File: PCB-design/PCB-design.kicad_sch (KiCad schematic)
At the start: 1 part, among them U1 UCC28070DW

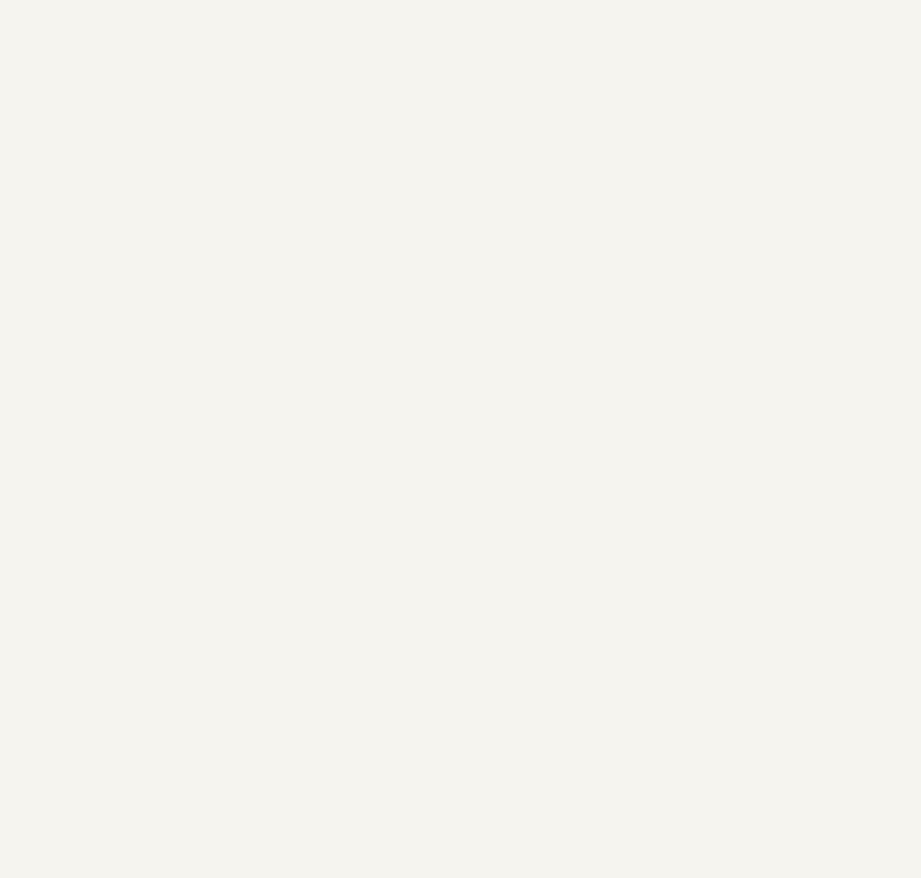
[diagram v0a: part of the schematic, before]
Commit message: New pin headers
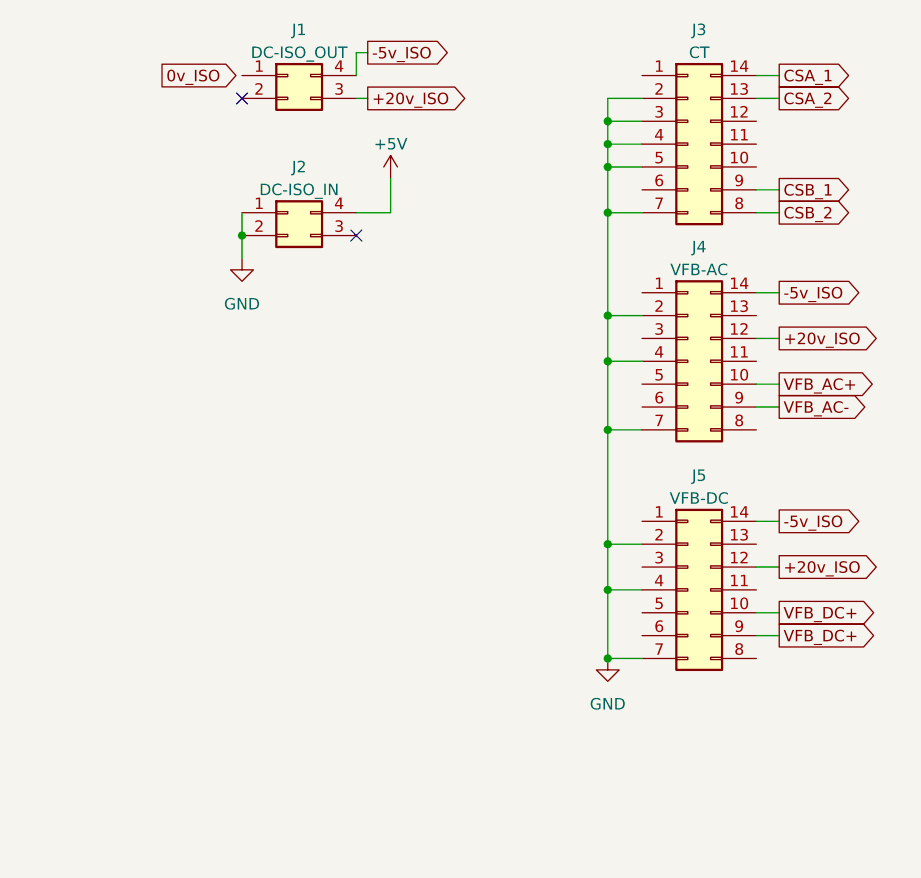
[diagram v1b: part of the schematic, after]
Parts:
- added J1: DC-ISO_OUT, symbol Connector_Generic:Conn_02x02_Counter_Clockwise
- added J2: DC-ISO_IN, symbol Connector_Generic:Conn_02x02_Counter_Clockwise
- added J3: CT, symbol Connector_Generic:Conn_02x07_Counter_Clockwise
- added J4: VFB-AC, symbol Connector_Generic:Conn_02x07_Counter_Clockwise
- added J5: VFB-DC, symbol Connector_Generic:Conn_02x07_Counter_Clockwise
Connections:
- new net +20v_ISO: J1.3 (Pin_3), J4.12 (Pin_12), J5.12 (Pin_12)
- new net +5V: J2.4 (Pin_4)
- new net -5v_ISO: J1.4 (Pin_4), J4.14 (Pin_14), J5.14 (Pin_14)
- new net CSA_1: J3.14 (Pin_14)
- new net CSA_2: J3.13 (Pin_13)
- new net CSB_1: J3.9 (Pin_9)
- new net CSB_2: J3.8 (Pin_8)
- new net GND: J2.1 (Pin_1), J2.2 (Pin_2), J3.2 (Pin_2), J3.3 (Pin_3), J3.4 (Pin_4), J3.5 (Pin_5), J3.7 (Pin_7), J4.2 (Pin_2), J4.4 (Pin_4), J4.7 (Pin_7), J5.2 (Pin_2), J5.4 (Pin_4), J5.7 (Pin_7)
- new net VFB_AC+: J4.10 (Pin_10)
- new net VFB_AC-: J4.9 (Pin_9)
- new net VFB_DC+: J5.10 (Pin_10), J5.9 (Pin_9)
- no-connect marks 0 -> 2

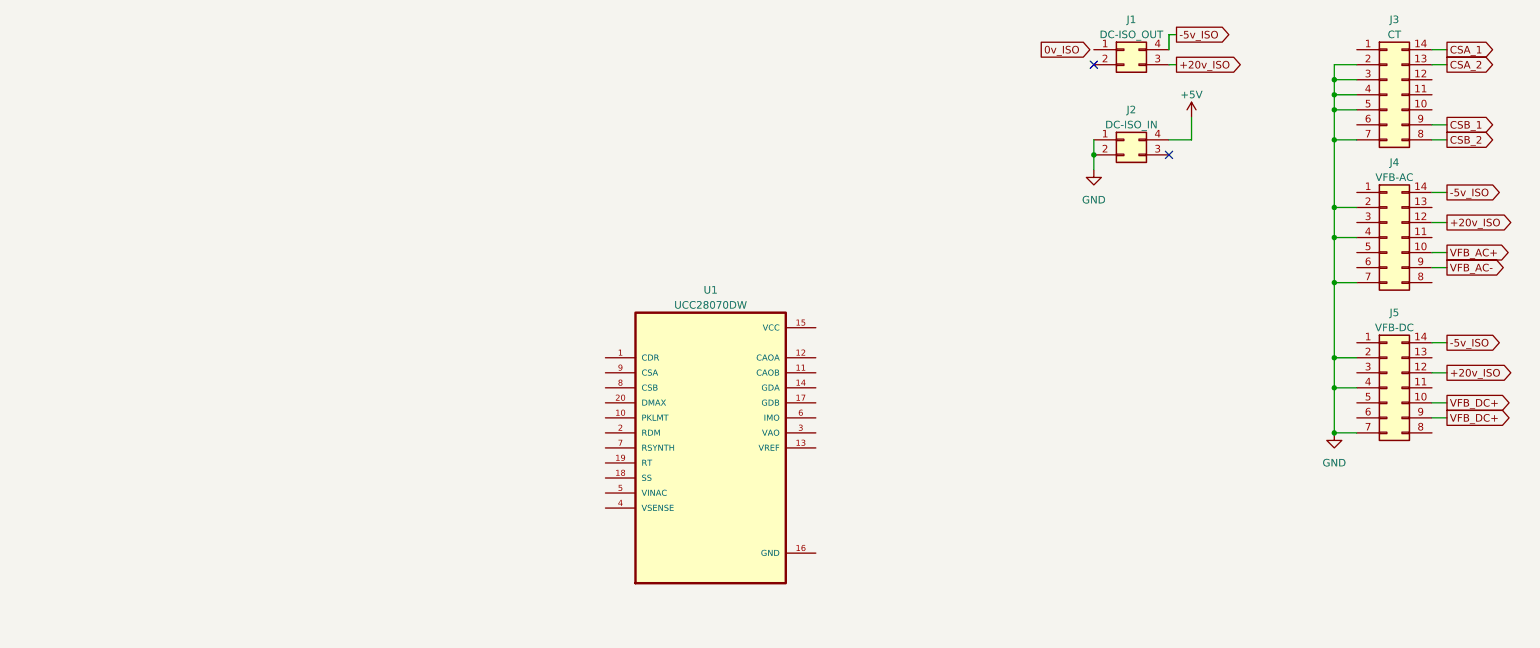
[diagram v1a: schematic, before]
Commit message: boost converter added: should probably double check
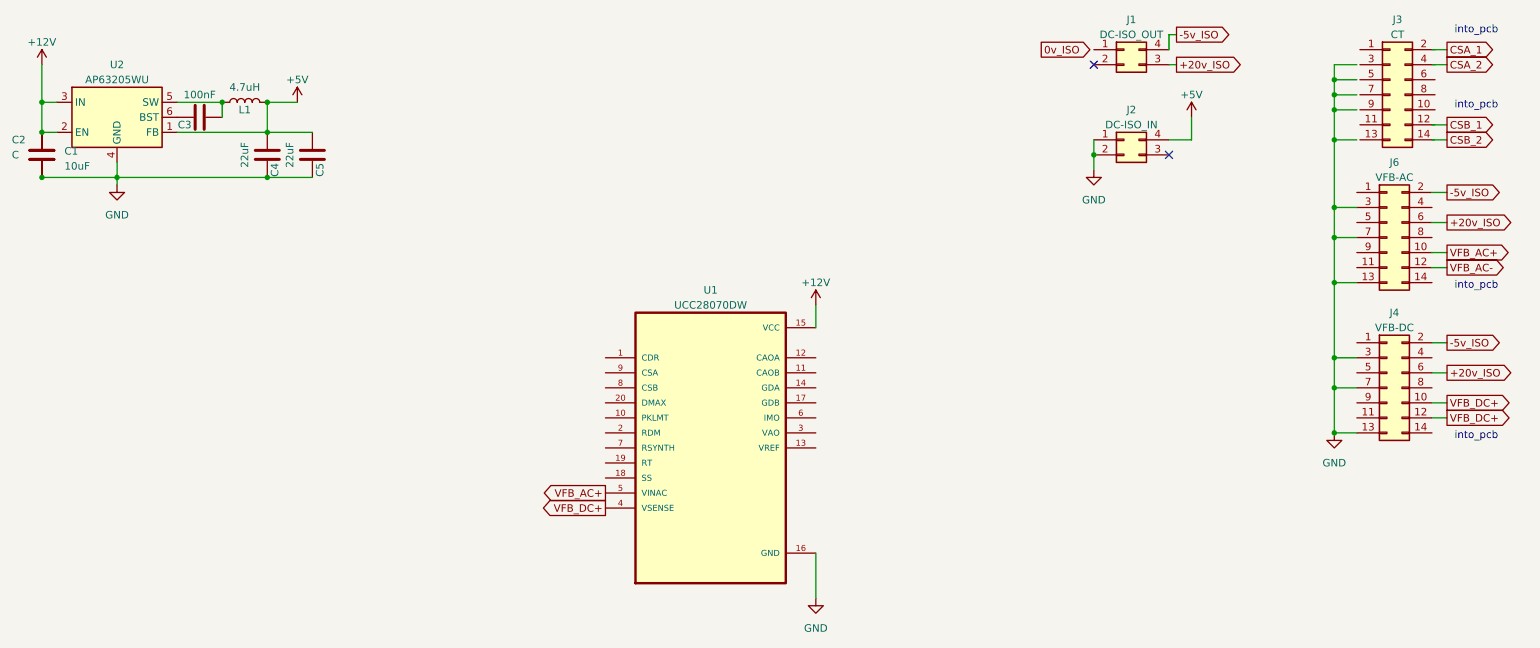
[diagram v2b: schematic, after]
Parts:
- removed J3: CT, symbol Connector_Generic:Conn_02x07_Counter_Clockwise
- removed J4: VFB-AC, symbol Connector_Generic:Conn_02x07_Counter_Clockwise
- removed J5: VFB-DC, symbol Connector_Generic:Conn_02x07_Counter_Clockwise
- added C1: 10uF, symbol Device:C
- added C2: C, symbol Device:C
- added C3: 100nF, symbol Device:C
- added C4, C5: 22uF, symbol Device:C
- added J3: CT, symbol Connector_Generic:Conn_02x07_Odd_Even
- added J4: VFB-DC, symbol Connector_Generic:Conn_02x07_Odd_Even
- added J6: VFB-AC, symbol Connector_Generic:Conn_02x07_Odd_Even
- added L1: 4.7uH, symbol Device:L
- added U2: AP63205WU, Package_TO_SOT_SMD:TSOT-23-6, symbol Regulator_Switching:AP63205WU
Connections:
- net +20v_ISO: now also J4.6 (Pin_6), J6.6 (Pin_6)
- net +5V: now also C4.2, C5.2, L1.2, U2.1 (FB)
- net -5v_ISO: now also J4.2 (Pin_2), J6.2 (Pin_2)
- net GND: now also U1.16 (GND), C1.2, C2.2, C4.1, C5.1, J4.13 (Pin_13), J4.3 (Pin_3), J4.7 (Pin_7), J6.13 (Pin_13), J6.3 (Pin_3), J6.7 (Pin_7), U2.4 (GND)
- net VFB_AC+: now also U1.5 (VINAC), J6.10 (Pin_10)
- net VFB_AC-: now also J6.12 (Pin_12)
- net VFB_DC+: now also U1.4 (VSENSE), J4.10 (Pin_10), J4.12 (Pin_12)
- net +12V: now reaches U1.15 (VCC)
- net +12V: now also C1.1, C2.1, U2.2 (EN), U2.3 (IN)
- new net: C3.2, L1.1, U2.5 (SW)
- new net: C3.1, U2.6 (BST)
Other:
- note added: "into_pcb"

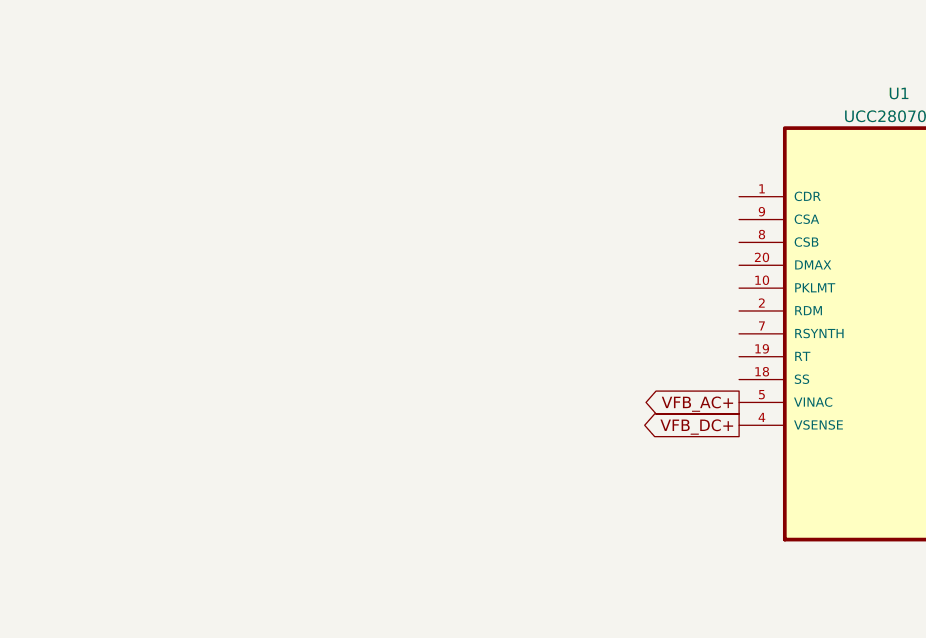
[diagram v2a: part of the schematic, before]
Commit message: structuring IC pins
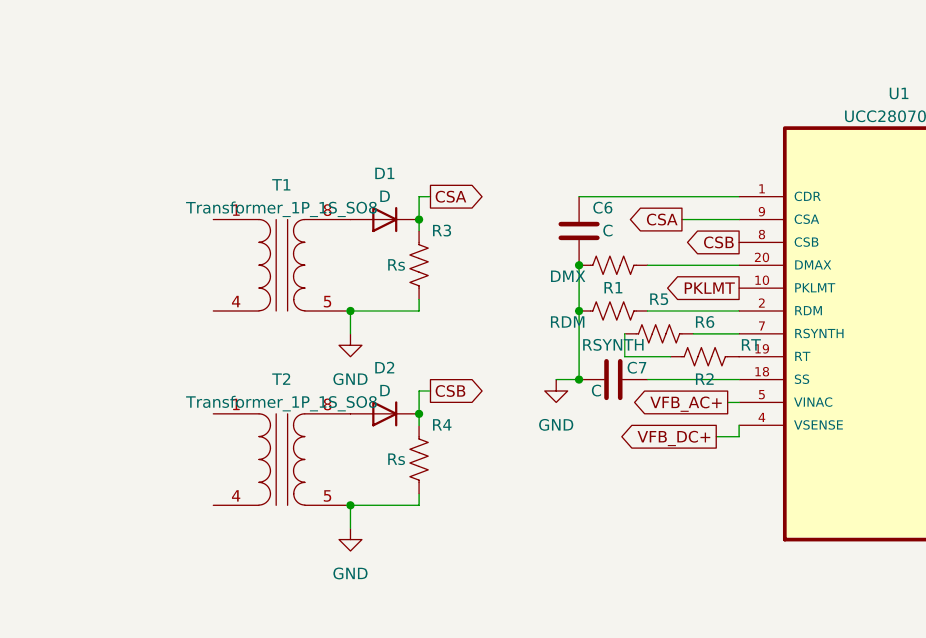
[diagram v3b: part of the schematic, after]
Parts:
- added C6, C7: C, symbol Device:C
- added D1, D2: D, symbol Device:D
- added R1: DMX, symbol Device:R_US
- added R2: RT, symbol Device:R_US
- added R3, R4: Rs, symbol Device:R_US
- added R5: RDM, symbol Device:R_US
- added R6: RSYNTH, symbol Device:R_US
- added T1, T2: Transformer_1P_1S_SO8, symbol Device:Transformer_1P_1S_SO8
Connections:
- net GND: now also C6.1, C7.1, R1.2, R3.2, R4.2, R5.2, T1.5 (SA), T2.5 (SA)
- net at U1.1 (CDR): now also C6.2
- net PKLMT: now reaches U1.10 (PKLMT)
- net at U1.18 (SS): now also C7.2
- net at U1.19 (RT): now also R2.1
- net at U1.2 (RDM): now also R5.1
- net at U1.20 (DMAX): now also R1.1
- net at U1.7 (RSYNTH): now also R6.1
- net CSB: now reaches U1.8 (CSB)
- net CSB: now also D2.1 (K), R4.1
- net CSA: now reaches U1.9 (CSA)
- net CSA: now also D1.1 (K), R3.1
- new net: D1.2 (A), T1.8 (SB)
- new net: R2.2, R6.2
- new net: D2.2 (A), T2.8 (SB)

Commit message: connections to APFC IC
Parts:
- added C10: Czv, symbol Device:C
- added C11, C13: Cpc, symbol Device:C
- added C12, C14: Czc, symbol Device:C
- added C8: Cref, symbol Device:C
- added C9: Cpv, symbol Device:C
- added R10, R8: RPK2, symbol Device:R_US
- added R11, R12: Rzc, symbol Device:R_US
- added R7: RPK1, symbol Device:R_US
- added R9: Rzv, symbol Device:R_US
- C6: value C -> Ccdr
- C7: value C -> Css
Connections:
- net CSA_1: now also J3.2 (Pin_2)
- net CSA_2: now also J3.4 (Pin_4)
- net CSB_1: now also J3.12 (Pin_12)
- net CSB_2: now also J3.14 (Pin_14)
- net GND: now also J3.13 (Pin_13), J3.3 (Pin_3), J3.5 (Pin_5), J3.7 (Pin_7), J3.9 (Pin_9), C11.1, C13.1, C8.1, C9.1, R10.1, R11.2, R12.1, R8.1, R9.2
- net PKLMT: now also R7.1, R8.2
- net at U1.11 (CAOB): now also C11.2, C12.2
- net at U1.12 (CAOA): now also C13.2, C14.2
- net at U1.13 (VREF): now also C8.2, R7.2
- net GDA: now reaches U1.14 (GDA)
- net GDB: now reaches U1.17 (GDB)
- net at U1.3 (VAO): now also C10.2, C9.2
- net at U1.6 (IMO): now also R10.2
- new net: C14.1, R12.2
- new net: C12.1, R11.1
- new net: C10.1, R9.1
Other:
- moved on the sheet: J3
